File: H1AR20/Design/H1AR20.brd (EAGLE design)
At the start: 34.6 x 30 mm, 42 parts, among them J1 67503-1020, P1 HEXABIT_17.32_NO_P3, U1 STM32F091CBU6, U2 LM3940IMP-3.3, U3 FT230XQ-R, X1 XTALL_CSTCE8M00G52

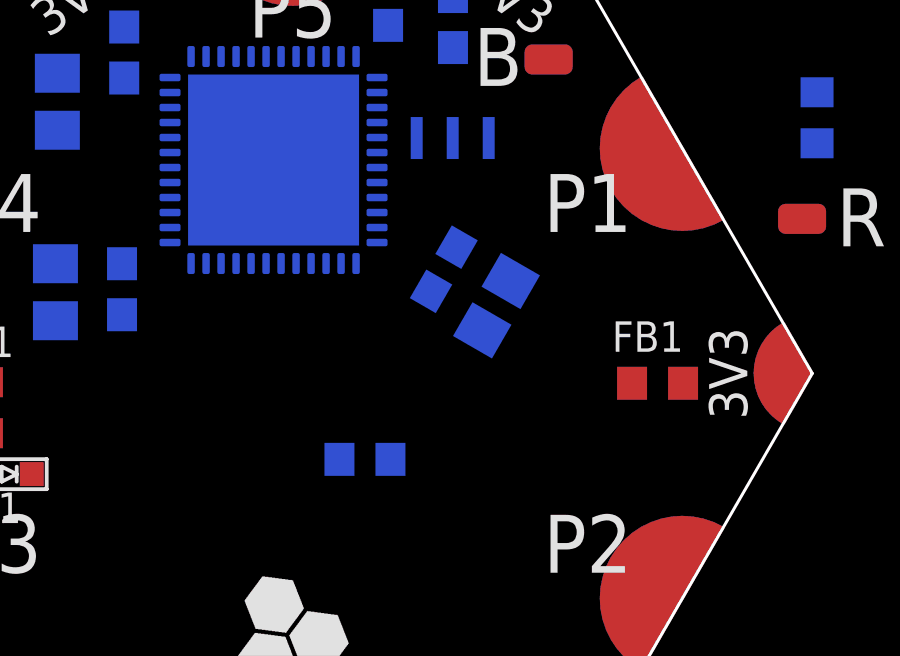
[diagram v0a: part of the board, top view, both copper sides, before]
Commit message: replaced labels "USART" with "UART"
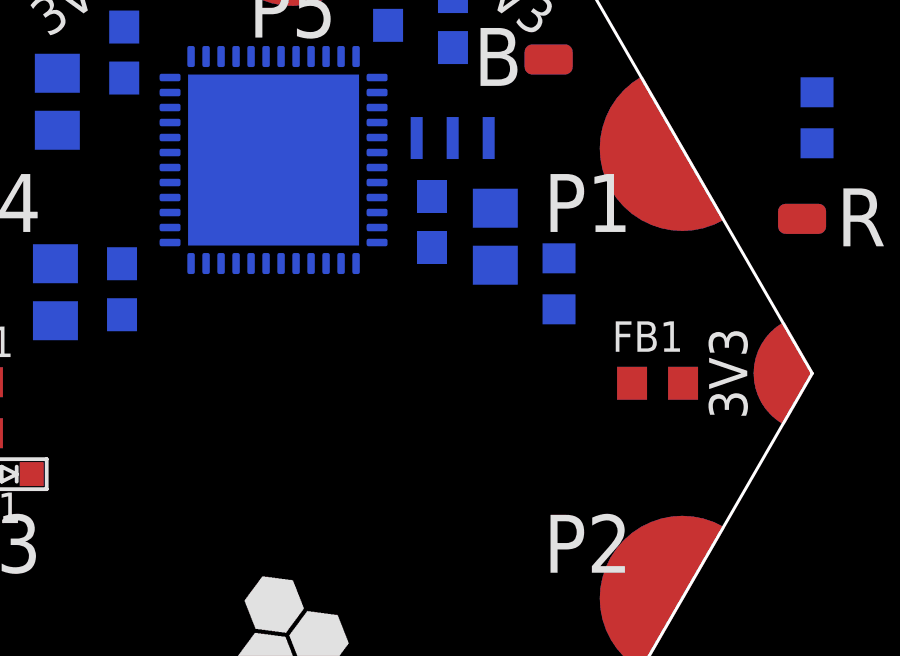
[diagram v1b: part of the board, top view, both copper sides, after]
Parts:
- moved R3 8.72 mm to (43.5, 37.6), turned to 90 degrees
- moved C2 2.30 mm to (41.4, 39.2), turned to 90 degrees
- moved C5 1.62 mm to (39.3, 39.7), turned to 90 degrees
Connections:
- net USART1_CTS renamed UART1_CTS
- net USART1_RTS renamed UART1_RTS
- net USART1_RX renamed UART1_RX
- net USART1_TX renamed UART1_TX
- net USART2_RX renamed UART2_RX
- net USART2_TX renamed UART2_TX
- net USART3_RX renamed UART3_RX
- net USART3_TX renamed UART3_TX
- net USART4_RX renamed UART4_RX
- net USART4_TX renamed UART4_TX
- net USART5_RX renamed UART5_RX
- net USART5_TX renamed UART5_TX
- net USART6_RX renamed UART6_RX
- net USART6_TX renamed UART6_TX

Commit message: - PCB is done - Generated all output files
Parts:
- removed JP1: (no value), jumper:JP1
- added J2: 3-644456-2, Hexabitz:TE_3-644456-2
- U2: value LM3940IMP-3.3 -> FT230XQ-R; device Hexabitz:SOT230P696X180-4N -> Hexabitz:QFN16
- U3: value FT230XQ-R -> LM3940IMP-3.3; device Hexabitz:QFN16 -> Hexabitz:SOT230P696X180-4N
- moved C10 92.4 mm to (33.0, 33.8), flipped to the bottom, turned to 90 degrees
- moved C12 91.1 mm to (35.0, 34.2), flipped to the bottom, turned to 90 degrees
- moved C11 84.1 mm to (38.3, 25.9), flipped to the bottom, turned to 270 degrees
- moved D2 77.9 mm to (42.2, 26.4), turned to 180 degrees
- moved R7 76.7 mm to (42.9, 30.8), flipped to the bottom, turned to 270 degrees
- moved D3 72.0 mm to (26.6, 26.3), turned to 180 degrees
- moved R6 71.4 mm to (35.6, 27.5), flipped to the bottom
- moved C15 70.0 mm to (40.4, 25.9), flipped to the bottom, turned to 270 degrees
- moved R5 65.7 mm to (39.7, 23.2), flipped to the bottom, turned to 180 degrees
- moved R4 59.7 mm to (34.3, 24.1), flipped to the bottom, turned to 180 degrees
- moved C13 58.3 mm to (37.0, 21.5), flipped to the bottom, turned to 270 degrees
- moved C14 56.3 mm to (33.4, 21.5), flipped to the bottom, turned to 270 degrees
- moved R9 54.7 mm to (32.3, 27.5), flipped to the bottom, turned to 180 degrees
- moved R8 54.1 mm to (32.3, 29.6), flipped to the bottom
- moved C17 52.6 mm to (27.1, 43.0), turned to 90 degrees
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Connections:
- new net N$8: U3.4
- net GND: now also U1.P$19, U1.P$27, U1.P$3, U1.P$38, U2.13, U2.17, U2.3, U3.2; no longer U2.2, U2.4, U3.13, U3.17, U3.3
- net N$10: now also J2.2; no longer JP1.2
- net N$11: now also U3.1; no longer U2.1
- net N$12: now also U2.6; no longer U3.6
- net N$13: now also U2.7; no longer U3.7
- net N$14: now also U2.5; no longer U3.5
- net N$15: now also U2.11; no longer U3.11
- net N$18: now also J2.1; no longer JP1.1
- net UART1_CTS: now also U2.16; no longer U3.16
- net UART1_RTS: now also U2.4; no longer U3.4
- net UART1_RX: now also U2.15; no longer U3.15
- net UART1_TX: now also U2.2; no longer U3.2
- net VBUS_SENSE: now also U2.14; no longer U3.14
- net VDD: now also U2.1, U2.10, U2.8, U2.9, U3.3; no longer U2.3, U3.1, U3.10, U3.8, U3.9
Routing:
- net VDD: track 0.00 -> 49.7 mm, vias 0 -> 6
- net GND: track 0.00 -> 48.7 mm, vias 0 -> 5
- net UART4_RX: track 0.00 -> 26.8 mm, vias 0 -> 2
- net UART4_TX: track 0.00 -> 23.8 mm, vias 0 -> 1
- net UART1_CTS: track 0.00 -> 19.6 mm, vias 0 -> 2
- net UART1_RTS: track 0.00 -> 19.1 mm, vias 0 -> 2
- net UART1_RX: track 0.00 -> 18.7 mm, vias 0 -> 2
- net UART6_TX: track 0.00 -> 18.7 mm, vias 0 -> 1
- net UART6_RX: track 0.00 -> 18.4 mm
- net UART3_TX: track 0.00 -> 17.9 mm, vias 0 -> 1
- net N$9: track 0.00 -> 17.1 mm, vias 0 -> 2
- net UART3_RX: track 0.00 -> 16.0 mm, vias 0 -> 2
- net N$7: track 0.00 -> 15.5 mm, vias 0 -> 1
- net UART1_TX: track 0.00 -> 15.1 mm, vias 0 -> 2
- net UART2_RX: track 0.00 -> 14.7 mm, vias 0 -> 2
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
